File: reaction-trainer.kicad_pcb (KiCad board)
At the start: 2 copper layers, 58 x 58 mm, 57 parts, among them J1 TC2050, J2 DNP, J3 DNP, J5 JST_PH_B2B, J6 47590-0001, U1 CH32V208WBU6, U2 MCP73831-2-OT, U3 HT7533-1, U4 74HC573PW,118, U5 LIS3DHTR, U6 USBLC6-2SC6, Y1 32MHz, Y2 32768Hz

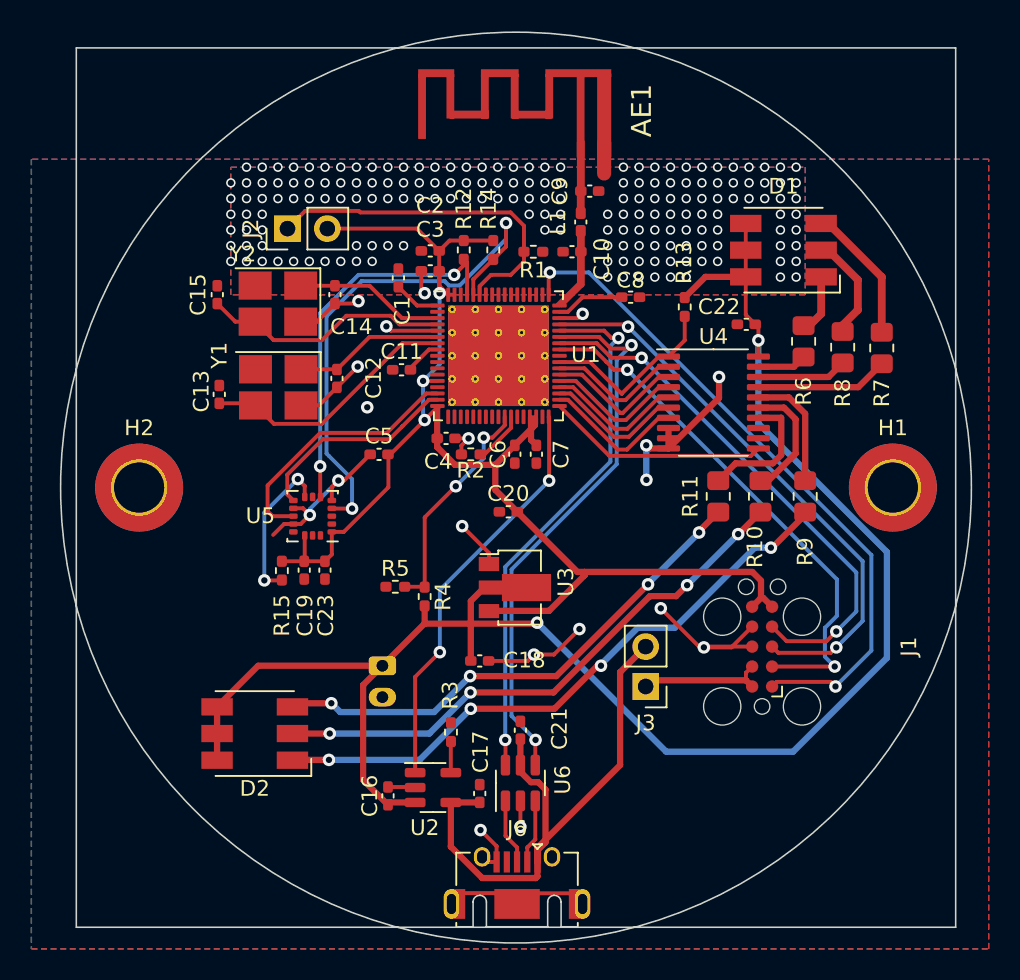
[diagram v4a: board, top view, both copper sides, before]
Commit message: Changed outline for DFM
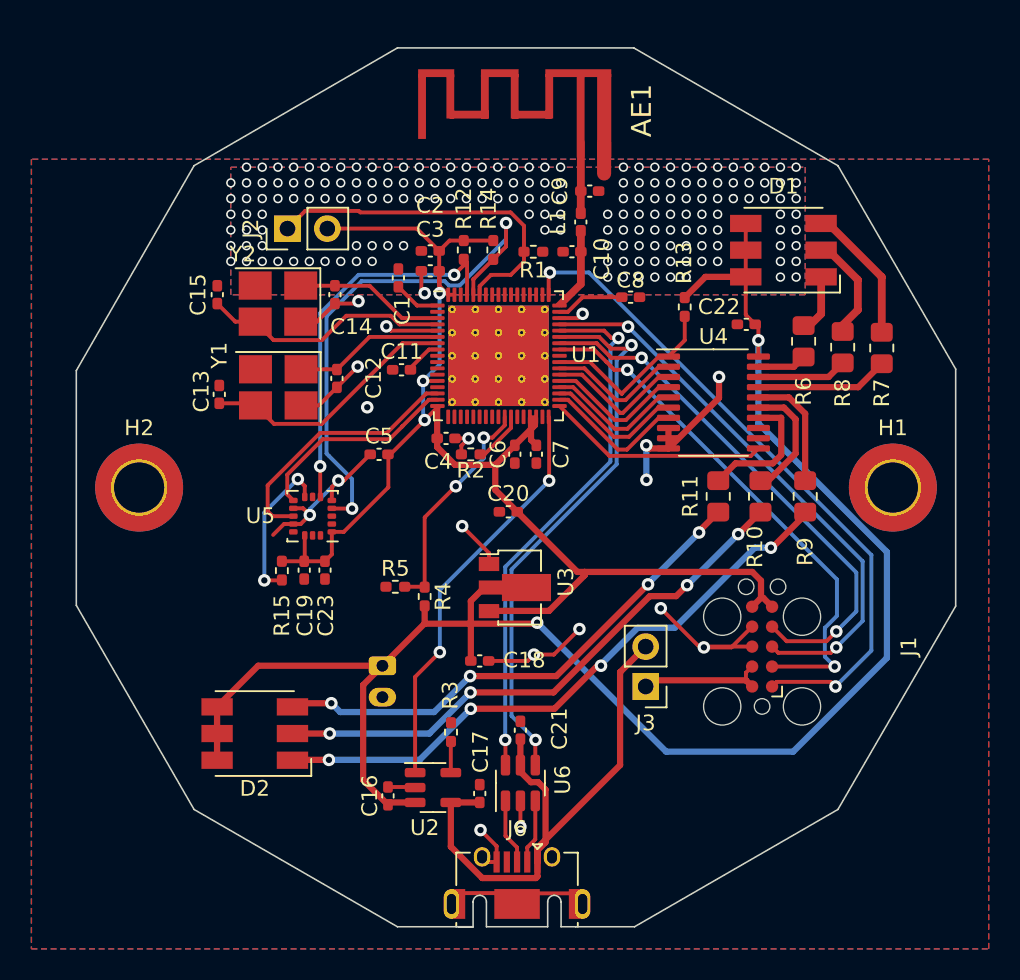
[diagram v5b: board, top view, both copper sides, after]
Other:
- board size 58 x 58 mm -> 56 x 56 mm
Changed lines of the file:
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@@
     )
   )
-  (gr_rect (start 107 62) (end 163 118)
-    (stroke (width 0.1) (type default)) (fill none) (layer "Edge.Cuts"))
-  (gr_circle (center 135 90) (end 164 90)
-    (stroke (width 0.1) (type default)) (fill none) (layer "Edge.Cuts"))
+  (gr_line (start 114.5 69.5) (end 127.45 62)
+    (stroke (width 0.1) (type default)) (layer "Edge.Cuts"))
+  (gr_line (start 127.45 62) (end 142.5 62)
+    (stroke (width 0.1) (type default)) (layer "Edge.Cuts"))
+  (gr_line (start 163 82.45) (end 163 97.55)
+    (stroke (width 0.1) (type default)) (layer "Edge.Cuts"))
+  (gr_line (start 155.5 110.5) (end 163 97.55)
+    (stroke (width 0.1) (type default)) (layer "Edge.Cuts"))
+  (gr_line (start 155.5 69.5) (end 142.5 62)
+    (stroke (width 0.1) (type default)) (layer "Edge.Cuts"))
+  (gr_line (start 107 82.55) (end 114.5 69.5)
+    (stroke (width 0.1) (type default)) (layer "Edge.Cuts"))
+  (gr_line (start 138.8168 117.9678) (end 142.55 117.9678)
+    (stroke (width 0.1) (type default)) (layer "Edge.Cuts"))
+  (gr_line (start 107 97.5) (end 107 82.55)
+    (stroke (width 0.1) (type default)) (layer "Edge.Cuts"))
+  (gr_line (start 107 97.5) (end 114.5 110.5)
+    (stroke (width 0.1) (type default)) (layer "Edge.Cuts"))
+  (gr_line (start 132.2668 117.9678) (end 127.45 117.9678)
+    (stroke (width 0.1) (type default)) (layer "Edge.Cuts"))
+  (gr_line (start 114.5 110.5) (end 127.45 117.9678)
+    (stroke (width 0.1) (type default)) (layer "Edge.Cuts"))
+  (gr_line (start 163 82.45) (end 155.5 69.5)
+    (stroke (width 0.1) (type default)) (layer "Edge.Cuts"))
+  (gr_line (start 142.55 117.9678) (end 155.5 110.5)
+    (stroke (width 0.1) (type default)) (layer "Edge.Cuts"))
   (segment (start 139.125258 71.123024) (end 139.128282 71.12) (width 0.25) (layer "F.Cu") (net 1))
   (segment (start 139.125258 72.515) (end 139.125258 71.123024) (width 0.5) (layer "F.Cu") (net 1))
